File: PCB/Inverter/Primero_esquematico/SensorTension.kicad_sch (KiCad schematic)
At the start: 74 parts, among them U14 AMC1301QDWVRQ1, U15 AMC1301QDWVRQ1, U16 AMC1301QDWVRQ1, U17 AMC1301QDWVRQ1, U18 TLV9004QDRQ1, U19 ADR130BUJZ-REEL7

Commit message: Esquematico practicamente terminado
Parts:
- added C113: 100nF, Capacitor_SMD:C_0603_1608Metric, symbol Device:C_Small
- C64, C65, C66, C67, C68, C69, C70: footprint (none) -> Capacitor_SMD:C_0603_1608Metric
- R100, R101, R102, R103, R104, R105, R106, R107, R108, R109, R78, R79, R80, R81, R82, R83, R84, R85, R86, R87, R88, R89, R90, R91, R92, R93, R94, R95, R96, R97, R98, R99: footprint (none) -> Resistor_SMD:R_0805_2012Metric
- R110, R111, R112, R113, R114, R115, R116, R117, R118, R119, R120, R121, R122, R123, R124, R125, R126, R127, R128, R129, R130, R131, R132, R133: footprint (none) -> Resistor_SMD:R_0402_1005Metric
- TP1, TP2, TP3, TP4: footprint (none) -> TestPoint:TestPoint_Pad_D2.0mm
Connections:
- net +3.3V renamed +3.3VA
- net 1.65V_ref renamed +1VA5
- net +1VA5: now also C113.1
- net GND renamed GND1
- net GND1: now also C113.2

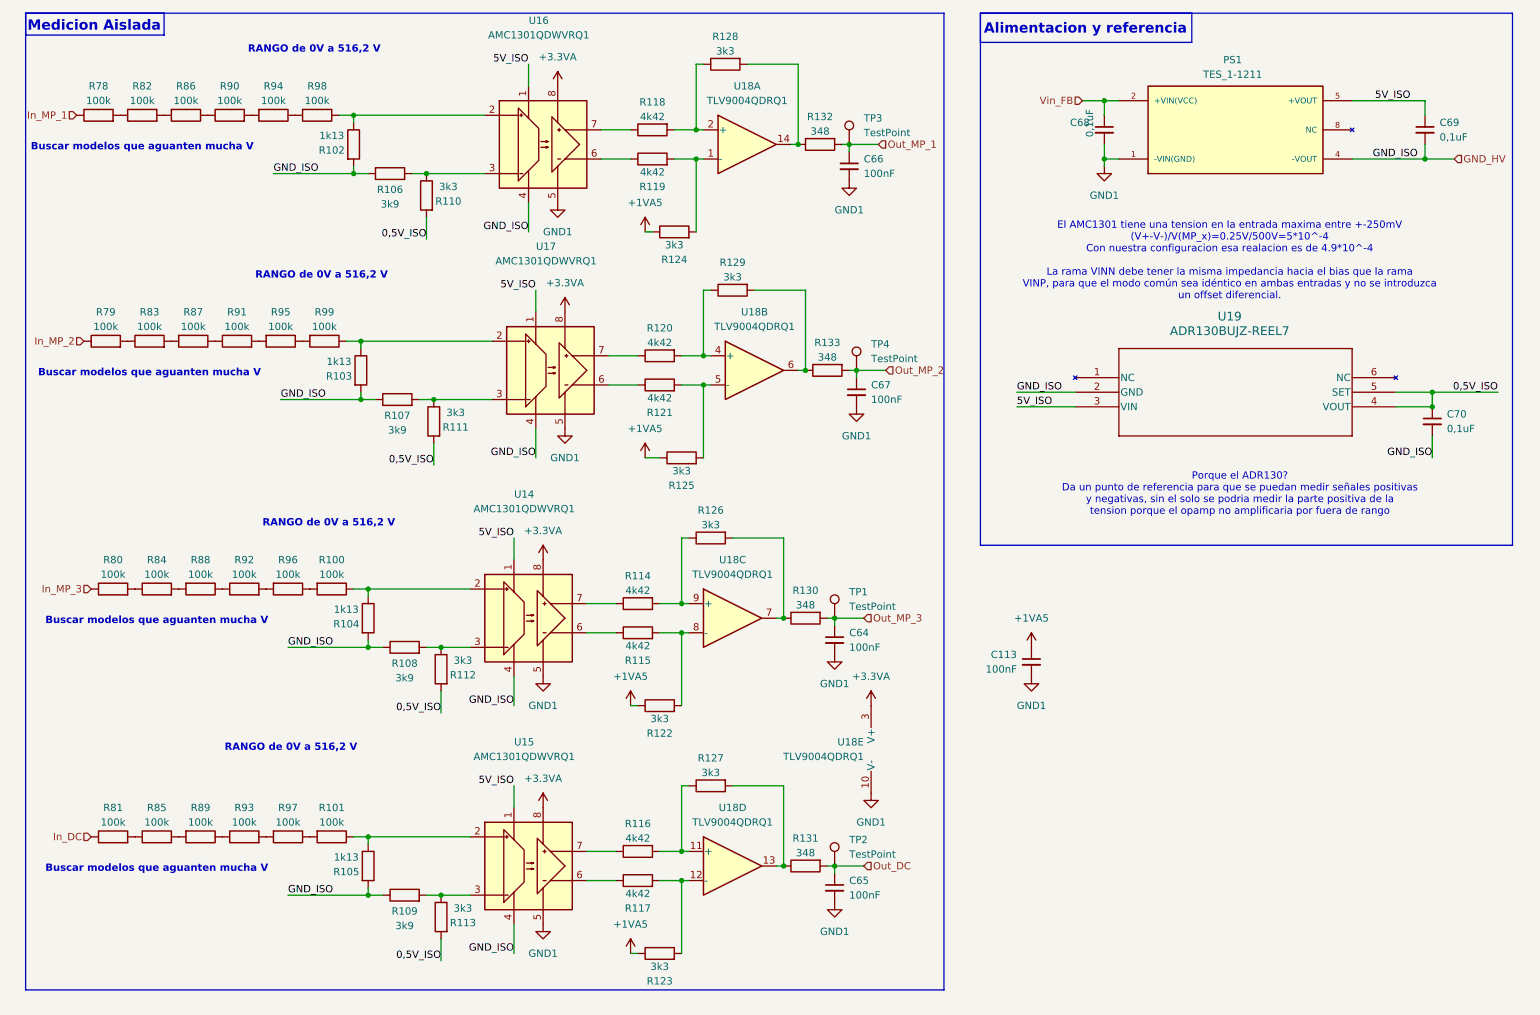
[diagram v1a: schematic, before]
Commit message: Un par de cosas q corregi del ERC pero sigue mal
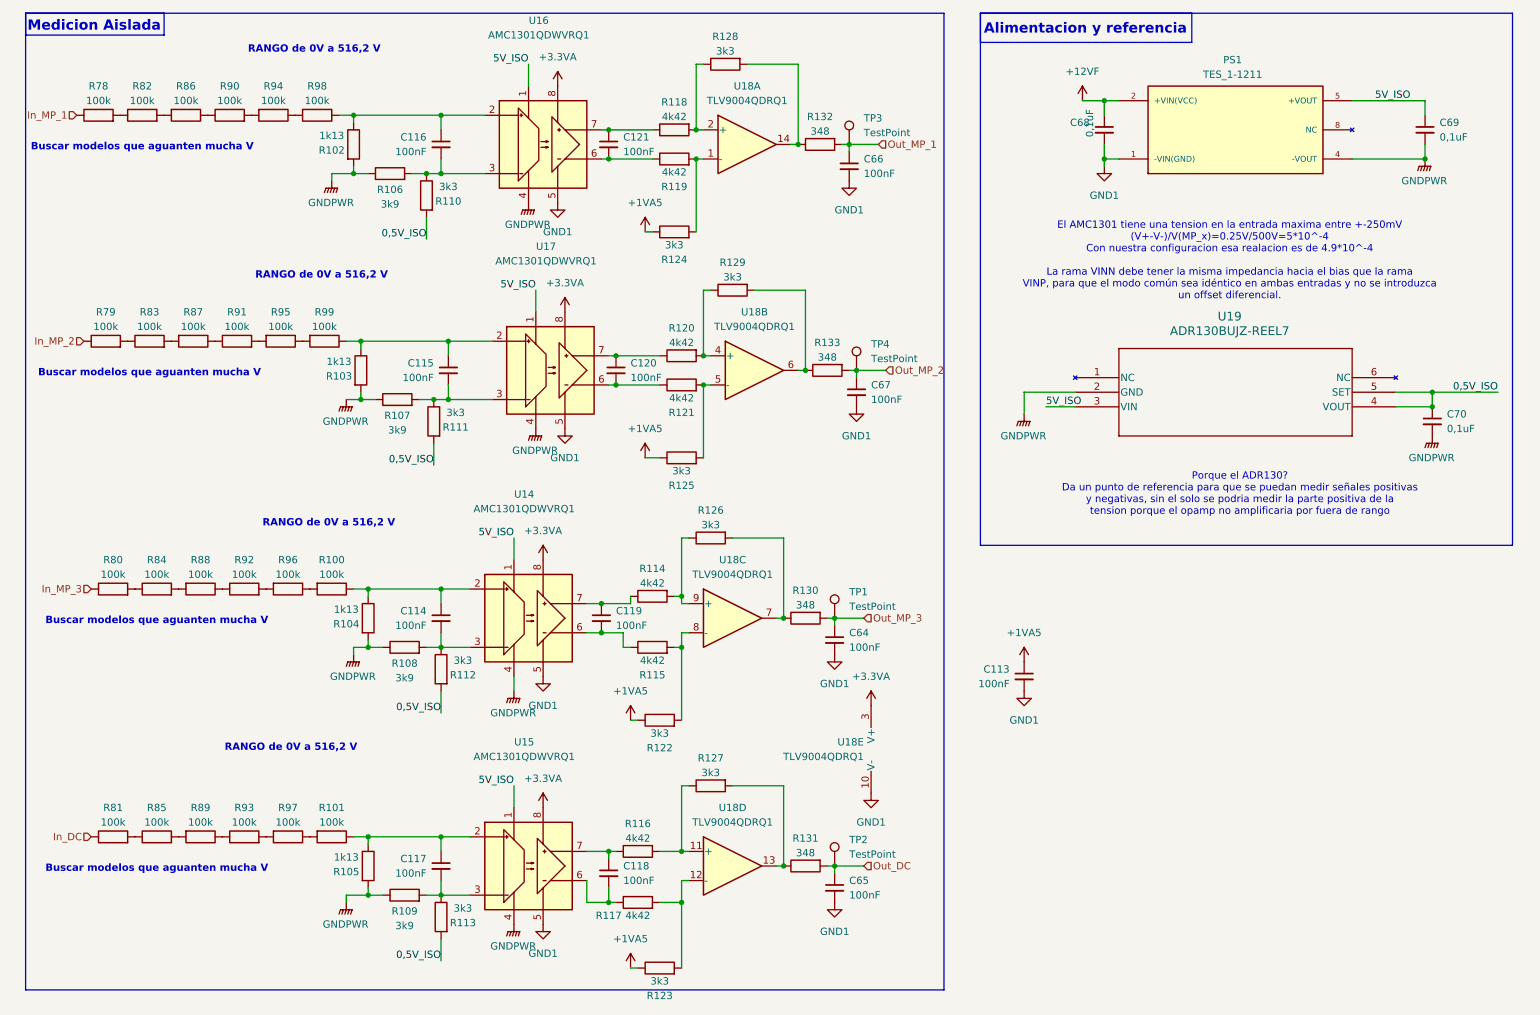
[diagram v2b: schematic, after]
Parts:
- added C114, C115, C116, C117, C118, C119, C120, C121: 100nF, Capacitor_SMD:C_0603_1608Metric, symbol Device:C_Small
- U18: footprint Package_SO:SOIC-14_3.9x8.7mm_P1.27mm -> Package_DFN_QFN:Texas_S-PX2QFN-14
- U19: footprint Snapeda:UJ_6_ADI-L -> UJ_6_ADI
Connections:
- net at R107.2, R111.1, U17.3 (VINN): now also C115.2
- net at R106.2, R110.1, U16.3 (VINN): now also C116.2
- net at R103.1, R99.1, U17.2 (VINP): now also C115.1
- net at R115.1, U14.6 (VOUTN): now also C119.2
- net at R100.1, R104.1, U14.2 (VINP): now also C114.1
- net at R101.1, R105.1, U15.2 (VINP): now also C117.1
- net at R108.2, R112.1, U14.3 (VINN): now also C114.2
- net at R102.1, R98.1, U16.2 (VINP): now also C116.1
- net at R114.1, U14.7 (VOUTP): now also C119.1
- net at R121.1, U17.6 (VOUTN): now also C120.2
- net at R117.1, U15.6 (VOUTN): now also C118.2
- net at R119.1, U16.6 (VOUTN): now also C121.2
- net at R120.1, U17.7 (VOUTP): now also C120.1
- net at R109.2, R113.1, U15.3 (VINN): now also C117.2
- net at R116.1, U15.7 (VOUTP): now also C118.1
- net at R118.1, U16.7 (VOUTP): now also C121.1
- net GND_HV renamed GNDPWR
- net Vin_FB renamed +12VF
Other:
- moved on the sheet: C113, R114, R115, R117, R118, R119, R120, R121, R122, R123

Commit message: Esquematico Listo
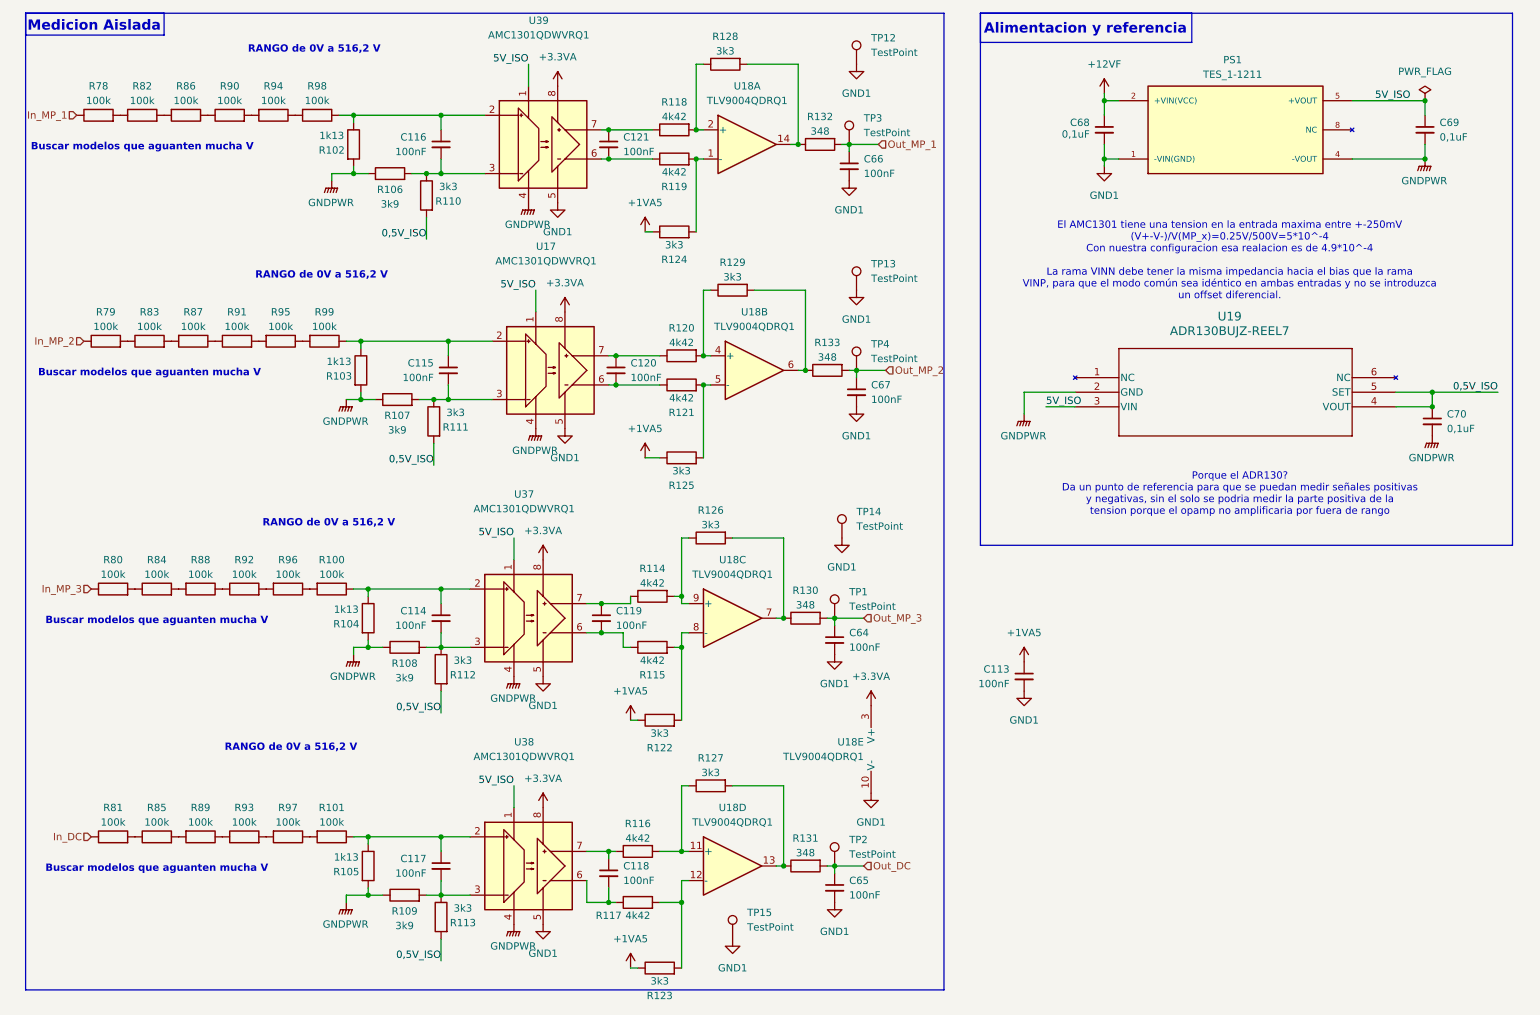
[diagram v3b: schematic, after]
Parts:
- removed U14, U15, U16: AMC1301QDWVRQ1, Package_SO:SOIC-8_7.5x5.85mm_P1.27mm, symbol Isolator_Analog:AMC1300DWV
- added TP12, TP13, TP14, TP15: TestPoint, TestPoint:TestPoint_Pad_D2.0mm, symbol Connector:TestPoint
- added U37, U38, U39: AMC1301QDWVRQ1, Package_SO:SOIC-8_7.5x5.85mm_P1.27mm, symbol Isolator_Analog:AMC1300DWV
- U19: footprint UJ_6_ADI -> NuevoGui:UJ_6_ADI-L
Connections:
- net +3.3VA: now also U37.8 (VDD2), U38.8 (VDD2), U39.8 (VDD2)
- net 5V_ISO: now also U37.1 (VDD1), U38.1 (VDD1), U39.1 (VDD1)
- net GND1: now also TP12.1, TP13.1, TP14.1, TP15.1, U37.5 (GND2), U38.5 (GND2), U39.5 (GND2)
- net GNDPWR: now also U37.4 (GND1), U38.4 (GND1), U39.4 (GND1)
- net at C117.1, R101.1, R105.1: now also U38.2 (VINP)
- net at C117.2, R109.2, R113.1: now also U38.3 (VINN)
- net at C116.2, R106.2, R110.1: now also U39.3 (VINN)
- net at C119.2, R115.1: now also U37.6 (VOUTN)
- net at C114.1, R100.1, R104.1: now also U37.2 (VINP)
- net at C114.2, R108.2, R112.1: now also U37.3 (VINN)
- net at C116.1, R102.1, R98.1: now also U39.2 (VINP)
- net at C119.1, R114.1: now also U37.7 (VOUTP)
- net at C118.2, R117.1: now also U38.6 (VOUTN)
- net at C121.2, R119.1: now also U39.6 (VOUTN)
- net at C118.1, R116.1: now also U38.7 (VOUTP)
- net at C121.1, R118.1: now also U39.7 (VOUTP)

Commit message: Sigo con la placa padre
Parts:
- R110, R111, R112, R113: footprint Resistor_SMD:R_0402_1005Metric -> Resistor_SMD:R_0805_2012Metric
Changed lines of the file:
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@@
 			)
 		)
-		(property "Footprint" "Resistor_SMD:R_0402_1005Metric"
+		(property "Footprint" "Resistor_SMD:R_0805_2012Metric"
 			(at 89.408 132.08 90)
 			(hide yes)
@@
 			)
 		)
-		(property "Footprint" "Resistor_SMD:R_0402_1005Metric"
+		(property "Footprint" "Resistor_SMD:R_0805_2012Metric"
 			(at 86.868 49.53 90)
 			(hide yes)
@@
 			)
 		)
-		(property "Footprint" "Resistor_SMD:R_0402_1005Metric"
+		(property "Footprint" "Resistor_SMD:R_0805_2012Metric"
 			(at 88.138 88.9 90)
 			(hide yes)
@@
 			)
 		)
-		(property "Footprint" "Resistor_SMD:R_0402_1005Metric"
+		(property "Footprint" "Resistor_SMD:R_0805_2012Metric"
 			(at 89.408 175.26 90)
 			(hide yes)

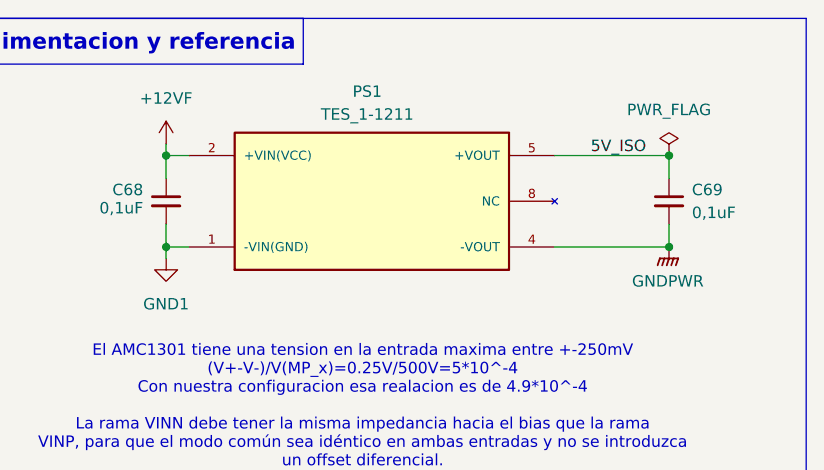
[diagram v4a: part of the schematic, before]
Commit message: Ordene los gate drivers
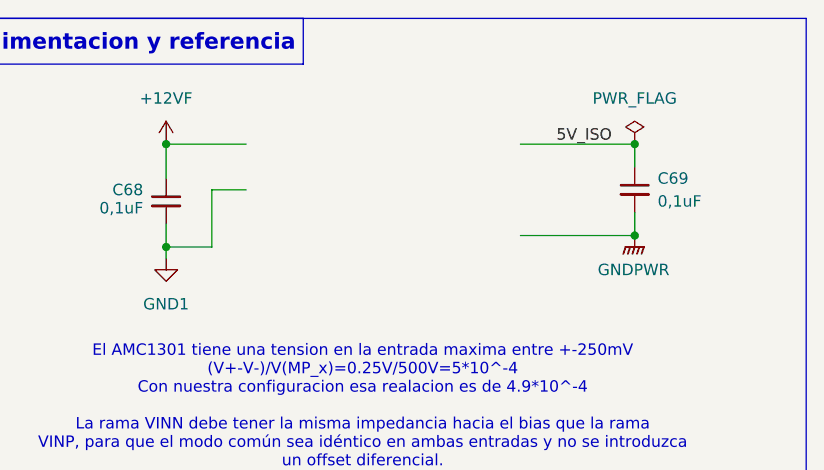
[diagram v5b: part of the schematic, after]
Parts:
- removed PS1: TES_1-1211, Snapeda:CONV_TES_1-1211, symbol Snapeda:TES_1-1211
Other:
- moved on the sheet: C69
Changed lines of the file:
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@@
 	)
 	(junction
-		(at 259.08 33.02)
+		(at 255.27 31.75)
 		(diameter 0)
 		(color 0 0 0 0)
@@
 	)
 	(junction
-		(at 203.2 33.02)
+		(at 203.2 31.75)
 		(diameter 0)
 		(color 0 0 0 0)
@@
 	)
 	(junction
-		(at 259.08 43.18)
+		(at 255.27 41.91)
 		(diameter 0)
 		(color 0 0 0 0)
@@
 	(wire
 		(pts
+			(xy 208.28 43.18) (xy 208.28 36.83)
+		)
+		(stroke
+			(width 0)
+			(type default)
+		)
+	)
+	(wire
+		(pts
 			(xy 72.39 118.11) (xy 74.93 118.11)
 		)
@@
 	(wire
 		(pts
-			(xy 205.74 43.18) (xy 203.2 43.18)
+			(xy 203.2 43.18) (xy 208.28 43.18)
 		)
 		(stroke
@@
 	(wire
 		(pts
-			(xy 203.2 33.02) (xy 203.2 35.56)
-		)
-		(stroke
-			(width 0)
-			(type default)
-		)
-	)
-	(wire
-		(pts
 			(xy 113.03 125.73) (xy 115.57 125.73)
 		)
@@
 	(wire
 		(pts
-			(xy 259.08 35.56) (xy 259.08 33.02)
+			(xy 255.27 34.29) (xy 255.27 31.75)
+		)
+		(stroke
+			(width 0)
+			(type default)
+		)
+	)
+	(wire
+		(pts
+			(xy 208.28 36.83) (xy 212.09 36.83)
 		)
 		(stroke
@@
 	(wire
 		(pts
-			(xy 203.2 33.02) (xy 205.74 33.02)
+			(xy 203.2 31.75) (xy 212.09 31.75)
 		)
 		(stroke
@@
 	(wire
 		(pts
-			(xy 246.38 43.18) (xy 259.08 43.18)
+			(xy 242.57 41.91) (xy 255.27 41.91)
 		)
 		(stroke
@@
 	(wire
 		(pts
-			(xy 246.38 33.02) (xy 259.08 33.02)
+			(xy 242.57 31.75) (xy 255.27 31.75)
 		)
 		(stroke
@@
 	(wire
 		(pts
-			(xy 259.08 40.64) (xy 259.08 43.18)
+			(xy 255.27 39.37) (xy 255.27 41.91)
 		)
 		(stroke
@@
 	(wire
 		(pts
-			(xy 203.2 31.75) (xy 203.2 33.02)
-		)
-		(stroke
-			(width 0)
-			(type default)
-		)
-	)
-	(wire
-		(pts
 			(xy 74.93 127) (xy 74.93 128.27)
 		)
@@
 		)
 	)
+	(wire
+		(pts
+			(xy 203.2 31.75) (xy 203.2 35.56)
+		)
+		(stroke
+			(width 0)
+			(type default)
+		)
+	)
 	(image
 		(at 234.2978 134.223)
@@
 	)
 	(label "5V_ISO"
-		(at 256.54 33.02 180)
+		(at 252.73 31.75 180)
 		(effects
 			(font
@@
 	(symbol
 		(lib_id "power:PWR_FLAG")
-		(at 259.08 33.02 0)
+		(at 255.27 31.75 0)
 		(unit 1)
 		(body_style 1)
@@
 		(fields_autoplaced yes)
 		(property "Reference" "#FLG06"
-			(at 259.08 31.115 0)
+			(at 255.27 29.845 0)
 			(hide yes)
 			(show_name no)
@@
 		)
 		(property "Value" "PWR_FLAG"
-			(at 259.08 27.94 0)
+			(at 255.27 26.67 0)
 			(show_name no)
 			(do_not_autoplace no)
@@
 		)
 		(property "Footprint" ""
-			(at 259.08 33.02 0)
+			(at 255.27 31.75 0)
 			(hide yes)
 			(show_name no)
@@
 		)
 		(property "Datasheet" ""
-			(at 259.08 33.02 0)
+			(at 255.27 31.75 0)
 			(hide yes)
 			(show_name no)
@@
 		)
 		(property "Description" "Special symbol for telling ERC where power comes from"
-			(at 259.08 33.02 0)
+			(at 255.27 31.75 0)
 			(hide yes)
 			(show_name no)
@@
 	(symbol
 		(lib_id "power:GNDPWR")
-		(at 259.08 43.18 0)
+		(at 255.27 41.91 0)
 		(unit 1)
 		(body_style 1)
@@
 		(fields_autoplaced yes)
 		(property "Reference" "#PWR0249"
-			(at 259.08 48.26 0)
+			(at 255.27 46.99 0)
 			(hide yes)
 			(show_name no)
@@
 		)
 		(property "Value" "GNDPWR"
-			(at 258.953 46.99 0)
+			(at 255.143 45.72 0)
 			(show_name no)
 			(do_not_autoplace no)
@@
 		)
 		(property "Footprint" ""
-			(at 259.08 44.45 0)
+			(at 255.27 43.18 0)
 			(hide yes)
 			(show_name no)
@@
 		)
 		(property "Datasheet" ""
-			(at 259.08 44.45 0)
+			(at 255.27 43.18 0)
 			(hide yes)
 			(show_name no)
@@
 		)
 		(property "Description" "Power symbol creates a global label with name \"GNDPWR\" , global ground"
-			(at 259.08 43.18 0)
+			(at 255.27 41.91 0)
 			(hide yes)
 			(show_name no)
@@
 	(symbol
 		(lib_id "Device:C_Small")
-		(at 259.08 38.1 0)
+		(at 255.27 36.83 0)
 		(unit 1)
 		(body_style 1)
@@
 		(fields_autoplaced yes)
 		(property "Reference" "C69"
-			(at 261.62 36.8362 0)
+			(at 257.81 35.5662 0)
 			(show_name no)
 			(do_not_autoplace no)
@@
 		)
 		(property "Value" "0,1uF"
-			(at 261.62 39.3762 0)
+			(at 257.81 38.1062 0)
 			(show_name no)
 			(do_not_autoplace no)
@@
 		)
 		(property "Footprint" "Capacitor_SMD:C_0603_1608Metric"
-			(at 259.08 38.1 0)
+			(at 255.27 36.83 0)
 			(hide yes)
 			(show_name no)
@@
 		)
 		(property "Datasheet" ""
-			(at 259.08 38.1 0)
+			(at 255.27 36.83 0)
 			(hide yes)
 			(show_name no)
@@
 		)
 		(property "Description" "Unpolarized capacitor, small symbol"
-			(at 259.08 38.1 0)
+			(at 255.27 36.83 0)
 			(hide yes)
 			(show_name no)
@@
 					(unit 1)
 				)
-			)
-		)
-	)
-	(symbol
-		(lib_id "Snapeda:TES_1-1211")
-		(at 226.06 38.1 0)
-		(unit 1)
-		(body_style 1)
-		(exclude_from_sim no)
-		(in_bom yes)
-		(on_board yes)
-		(in_pos_files yes)
-		(dnp no)
-		(property "Reference" "PS1"
-			(at 225.552 25.908 0)
-			(show_name no)
-			(do_not_autoplace no)
-			(effects
-				(font
-					(size 1.27 1.27)
-				)
-			)
-		)
-		(property "Value" "TES_1-1211"
-			(at 225.552 28.448 0)
-			(show_name no)
-			(do_not_autoplace no)
-			(effects
-				(font
-					(size 1.27 1.27)
-				)
-			)
-		)
-		(property "Footprint" "Snapeda:CONV_TES_1-1211"
-			(at 226.06 17.78 0)
-			(hide yes)
-			(show_name no)
-			(do_not_autoplace no)
-			(effects
-				(font
-					(size 1.27 1.27)
-				)
-			)
-		)
-		(property "Datasheet" ""
-			(at 226.06 38.1 0)
-			(hide yes)
-			(show_name no)
-			(do_not_autoplace no)
-			(effects
-				(font
-					(size 1.27 1.27)
-				)
-			)
-		)
-		(property "Description" "Isolated Module DC DC Converter 1 Output 5V 200mA 10.8V - 13.2V Input"
-			(at 226.06 38.1 0)
-			(hide yes)
-			(show_name no)
-			(do_not_autoplace no)
-			(effects
-				(font
-					(size 1.27 1.27)
-				)
-			)
-		)
-		(property "PARTREV" "July 12, 2024"
-			(at 226.06 20.32 0)
-			(hide yes)
-			(show_name no)
-			(do_not_autoplace no)
-			(effects
-				(font
-					(size 1.27 1.27)
-				)
-			)
-		)
-		(property "MANUFACTURER" "Traco Power"
-			(at 226.06 22.86 0)
-			(hide yes)
-			(show_name no)
-			(do_not_autoplace no)
-			(effects
-				(font
-					(size 1.27 1.27)
-				)
-			)
-		)
-		(property "MAXIMUM_PACKAGE_HEIGHT" "7.7mm"
-			(at 226.06 25.4 0)
-			(hide yes)
-			(show_name no)
-			(do_not_autoplace no)
-			(effects
-				(font
-					(size 1.27 1.27)
-				)
-			)
-		)
-		(property "STANDARD" "Manufacturer Recommendations"
-			(at 226.06 27.94 0)
-			(hide yes)
-			(show_name no)
-			(do_not_autoplace no)
-			(effects
-				(font
-					(size 1.27 1.27)
-				)
-			)
-		)
-		(property "Compra" "https://www.digikey.com/en/products/detail/traco-power/TES-1-1211/9382956"
-			(at 226.06 38.1 0)
-			(hide yes)
-			(show_name no)
-			(do_not_autoplace no)
-			(effects
-				(font
-					(size 1.27 1.27)
-				)
-			)
-		)
-		(pin "8"
-		)
-		(pin "2"
-		)
-		(pin "4"
-		)
-		(pin "5"
-		)
-		(pin "1"
-		)
-		(instances
-			(project "Primero_esquematico"
-				(path "/d930f486-f6ac-489c-907e-47f2cb34cf04/d101e913-ebd1-4e08-b728-82218f47123b/f5297dcd-d9e2-4174-98d4-ada2947e9df5/a3f260ee-b65b-4ad3-a336-2964f3b13ec0"
-					(reference "PS1")
-					(unit 1)
-				)
